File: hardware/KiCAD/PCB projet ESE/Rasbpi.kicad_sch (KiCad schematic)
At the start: 6 parts, among them J29 USB_C_Receptacle_USB2.0_16P, U5 USBLC6-2SC6

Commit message: maj schematic & pinout CubeIDE
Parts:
- renumbered J29 to J26, R30 to R22, R31 to R23
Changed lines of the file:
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@@
 		(dnp no)
 		(fields_autoplaced yes)
-		(property "Reference" "J29"
+		(property "Reference" "J26"
 			(at 90.17 69.85 0)
 			(effects
@@
 			(project ""
 				(path "/61bc2d2d-cd10-4636-b1b1-3d875f78e40b/7a080ce4-c82c-46c4-8a5a-914178d680a1"
-					(reference "J29")
+					(reference "J26")
 					(unit 1)
 				)
@@
 		(dnp no)
 		(fields_autoplaced yes)
-		(property "Reference" "#PWR0123"
+		(property "Reference" "#PWR0108"
 			(at 147.32 67.31 0)
 			(effects
@@
 			(project ""
 				(path "/61bc2d2d-cd10-4636-b1b1-3d875f78e40b/7a080ce4-c82c-46c4-8a5a-914178d680a1"
-					(reference "#PWR0123")
+					(reference "#PWR0108")
 					(unit 1)
 				)
@@
 		(dnp no)
 		(fields_autoplaced yes)
-		(property "Reference" "#PWR0121"
+		(property "Reference" "#PWR0106"
 			(at 124.46 91.44 0)
 			(effects
@@
 			(project ""
 				(path "/61bc2d2d-cd10-4636-b1b1-3d875f78e40b/7a080ce4-c82c-46c4-8a5a-914178d680a1"
-					(reference "#PWR0121")
+					(reference "#PWR0106")
 					(unit 1)
 				)
@@
 		(dnp no)
 		(fields_autoplaced yes)
-		(property "Reference" "#PWR0122"
+		(property "Reference" "#PWR0107"
 			(at 139.7 99.06 0)
 			(effects
@@
 			(project ""
 				(path "/61bc2d2d-cd10-4636-b1b1-3d875f78e40b/7a080ce4-c82c-46c4-8a5a-914178d680a1"
-					(reference "#PWR0122")
+					(reference "#PWR0107")
 					(unit 1)
 				)
@@
 		(on_board yes)
 		(dnp no)
-		(property "Reference" "R31"
+		(property "Reference" "R23"
 			(at 119.126 87.122 90)
 			(effects
@@
 			(project ""
 				(path "/61bc2d2d-cd10-4636-b1b1-3d875f78e40b/7a080ce4-c82c-46c4-8a5a-914178d680a1"
-					(reference "R31")
+					(reference "R23")
 					(unit 1)
 				)
@@
 		(dnp no)
 		(fields_autoplaced yes)
-		(property "Reference" "#PWR0120"
+		(property "Reference" "#PWR0105"
 			(at 86.36 121.92 0)
 			(effects
@@
 			(project ""
 				(path "/61bc2d2d-cd10-4636-b1b1-3d875f78e40b/7a080ce4-c82c-46c4-8a5a-914178d680a1"
-					(reference "#PWR0120")
+					(reference "#PWR0105")
 					(unit 1)
 				)
@@
 		(dnp no)
 		(fields_autoplaced yes)
-		(property "Reference" "R30"
+		(property "Reference" "R22"
 			(at 119.38 77.47 90)
 			(effects
@@
 			(project ""
 				(path "/61bc2d2d-cd10-4636-b1b1-3d875f78e40b/7a080ce4-c82c-46c4-8a5a-914178d680a1"
-					(reference "R30")
-					(unit 1)
-				)
+					(reference "R22")
+					(unit 1)
+				)

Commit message: maj
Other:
- moved on the sheet: F1, FB1, U5
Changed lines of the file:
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@@
 	(wire
 		(pts
-			(xy 123.19 63.5) (xy 134.62 63.5)
+			(xy 163.83 57.15) (xy 175.26 57.15)
 		)
 		(stroke
@@
 	(wire
 		(pts
-			(xy 147.32 63.5) (xy 139.7 63.5)
+			(xy 187.96 57.15) (xy 180.34 57.15)
 		)
 		(stroke
@@
 	(wire
 		(pts
-			(xy 118.11 63.5) (xy 115.57 63.5)
+			(xy 158.75 57.15) (xy 156.21 57.15)
 		)
 		(stroke
@@
 	(global_label "VBUS"
 		(shape input)
-		(at 115.57 63.5 180)
+		(at 156.21 57.15 180)
 		(fields_autoplaced yes)
 		(effects
@@
 		)
 		(property "Intersheetrefs" "${INTERSHEET_REFS}"
-			(at 107.2102 63.5 0)
+			(at 147.8502 57.15 0)
 			(effects
 				(font
@@
 	(global_label "D+"
 		(shape input)
-		(at 134.62 87.63 180)
+		(at 175.26 81.28 180)
 		(fields_autoplaced yes)
 		(effects
@@
 		)
 		(property "Intersheetrefs" "${INTERSHEET_REFS}"
-			(at 128.3164 87.63 0)
+			(at 168.9564 81.28 0)
 			(effects
 				(font
@@
 	(global_label "VBUS"
 		(shape input)
-		(at 139.7 80.01 90)
+		(at 180.34 73.66 90)
 		(fields_autoplaced yes)
 		(effects
@@
 		)
 		(property "Intersheetrefs" "${INTERSHEET_REFS}"
-			(at 139.7 71.6502 90)
+			(at 180.34 65.3002 90)
 			(effects
 				(font
@@
 	(global_label "D-"
 		(shape input)
-		(at 134.62 85.09 180)
+		(at 175.26 78.74 180)
 		(fields_autoplaced yes)
 		(effects
@@
 		)
 		(property "Intersheetrefs" "${INTERSHEET_REFS}"
-			(at 128.3164 85.09 0)
+			(at 168.9564 78.74 0)
 			(effects
 				(font
@@
 	(hierarchical_label "USB_DM"
 		(shape input)
-		(at 144.78 87.63 0)
+		(at 185.42 81.28 0)
 		(effects
 			(font
@@
 	(hierarchical_label "USB_DP"
 		(shape input)
-		(at 144.78 85.09 0)
+		(at 185.42 78.74 0)
 		(effects
 			(font
@@
 	(symbol
 		(lib_id "power:+5V")
-		(at 147.32 63.5 0)
+		(at 187.96 57.15 0)
 		(unit 1)
 		(exclude_from_sim no)
@@
 		(fields_autoplaced yes)
 		(property "Reference" "#PWR0108"
-			(at 147.32 67.31 0)
+			(at 187.96 60.96 0)
 			(effects
 				(font
@@
 		)
 		(property "Value" "+5V"
-			(at 147.32 58.42 0)
+			(at 187.96 52.07 0)
 			(effects
 				(font
@@
 		)
 		(property "Footprint" ""
-			(at 147.32 63.5 0)
+			(at 187.96 57.15 0)
 			(effects
 				(font
@@
 		)
 		(property "Datasheet" ""
-			(at 147.32 63.5 0)
+			(at 187.96 57.15 0)
 			(effects
 				(font
@@
 		)
 		(property "Description" "Power symbol creates a global label with name \"+5V\""
-			(at 147.32 63.5 0)
+			(at 187.96 57.15 0)
 			(effects
 				(font
@@
 	(symbol
 		(lib_id "Device:FerriteBead_Small")
-		(at 120.65 63.5 90)
+		(at 161.29 57.15 90)
 		(unit 1)
 		(exclude_from_sim no)
@@
 		(fields_autoplaced yes)
 		(property "Reference" "FB1"
-			(at 120.6119 57.15 90)
+			(at 161.2519 50.8 90)
 			(effects
 				(font
@@
 		)
 		(property "Value" "600 @ 100MHz"
-			(at 120.6119 59.69 90)
+			(at 161.2519 53.34 90)
 			(effects
 				(font
@@
 		)
 		(property "Footprint" "Inductor_SMD:L_0805_2012Metric"
-			(at 120.65 65.278 90)
+			(at 161.29 58.928 90)
 			(effects
 				(font
@@
 		)
 		(property "Datasheet" "~"
-			(at 120.65 63.5 0)
+			(at 161.29 57.15 0)
 			(effects
 				(font
@@
 		)
 		(property "Description" "Ferrite bead, small symbol"
-			(at 120.65 63.5 0)
+			(at 161.29 57.15 0)
 			(effects
 				(font
@@
 	(symbol
 		(lib_id "Device:Polyfuse_Small")
-		(at 137.16 63.5 90)
+		(at 177.8 57.15 90)
 		(unit 1)
 		(exclude_from_sim no)
@@
 		(fields_autoplaced yes)
 		(property "Reference" "F1"
-			(at 137.16 57.15 90)
+			(at 177.8 50.8 90)
 			(effects
 				(font
@@
 		)
 		(property "Value" "250mA"
-			(at 137.16 59.69 90)
+			(at 177.8 53.34 90)
 			(effects
 				(font
@@
 		)
 		(property "Footprint" "Fuse:Fuse_1206_3216Metric"
-			(at 142.24 62.23 0)
+			(at 182.88 55.88 0)
 			(effects
 				(font
@@
 		)
 		(property "Datasheet" "~"
-			(at 137.16 63.5 0)
+			(at 177.8 57.15 0)
 			(effects
 				(font
@@
 		)
 		(property "Description" "Resettable fuse, polymeric positive temperature coefficient, small symbol"
-			(at 137.16 63.5 0)
+			(at 177.8 57.15 0)
 			(effects
 				(font
@@
 	(symbol
 		(lib_id "power:GND")
-		(at 139.7 92.71 0)
+		(at 180.34 86.36 0)
 		(unit 1)
 		(exclude_from_sim no)
@@
 		(fields_autoplaced yes)
 		(property "Reference" "#PWR0107"
-			(at 139.7 99.06 0)
+			(at 180.34 92.71 0)
 			(effects
 				(font
@@
 		)
 		(property "Value" "GND"
-			(at 139.7 97.79 0)
+			(at 180.34 91.44 0)
 			(effects
 				(font
@@
 		)
 		(property "Footprint" ""
-			(at 139.7 92.71 0)
+			(at 180.34 86.36 0)
 			(effects
 				(font
@@
 		)
 		(property "Datasheet" ""
-			(at 139.7 92.71 0)
+			(at 180.34 86.36 0)
 			(effects
 				(font
@@
 		)
 		(property "Description" "Power symbol creates a global label with name \"GND\" , ground"
-			(at 139.7 92.71 0)
+			(at 180.34 86.36 0)
 			(effects
 				(font
@@
 	(symbol
 		(lib_id "Power_Protection:USBLC6-2SC6")
-		(at 139.7 85.09 0)
+		(at 180.34 78.74 0)
 		(unit 1)
 		(exclude_from_sim no)
@@
 		(fields_autoplaced yes)
 		(property "Reference" "U5"
-			(at 141.3511 77.47 0)
+			(at 181.9911 71.12 0)
 			(effects
 				(font
@@
 		)
 		(property "Value" "USBLC6-2SC6"
-			(at 141.3511 80.01 0)
+			(at 181.9911 73.66 0)
 			(effects
 				(font
@@
 		)
 		(property "Footprint" "Package_TO_SOT_SMD:SOT-23-6"
-			(at 140.97 91.44 0)
+			(at 181.61 85.09 0)
 			(effects
 				(font
@@
 		)
 		(property "Datasheet" "https://www.st.com/resource/en/datasheet/usblc6-2.pdf"
-			(at 140.97 93.345 0)
+			(at 181.61 86.995 0)
 			(effects
 				(font
@@
 		)
 		(property "Description" "Very low capacitance ESD protection diode, 2 data-line, SOT-23-6"
-			(at 139.7 85.09 0)
+			(at 180.34 78.74 0)
 			(effects
 				(font
@@
 		)
 		(property "MPN" "624-7693"
-			(at 139.7 85.09 0)
-			(effects
-				(font
+			(at 180.34 78.74 0)
+			(effects
+				(font

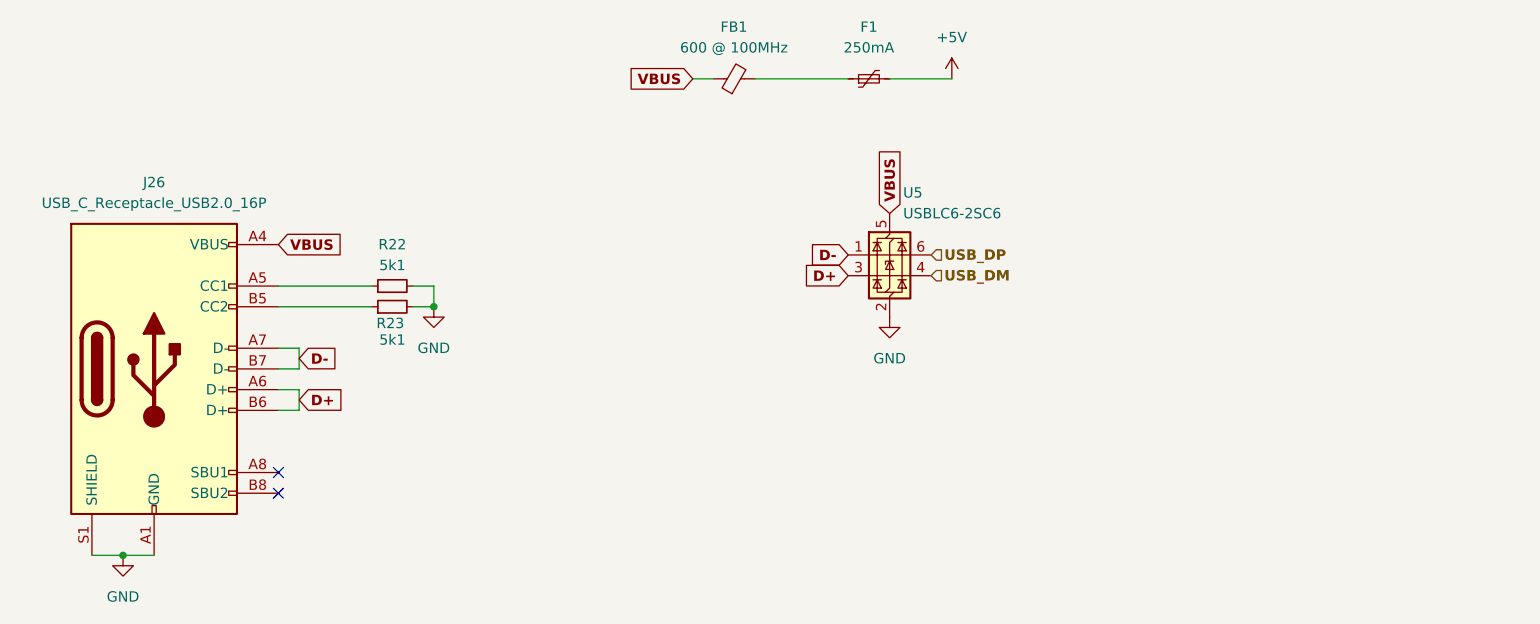
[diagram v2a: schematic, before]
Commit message: replace usb c by jst xh
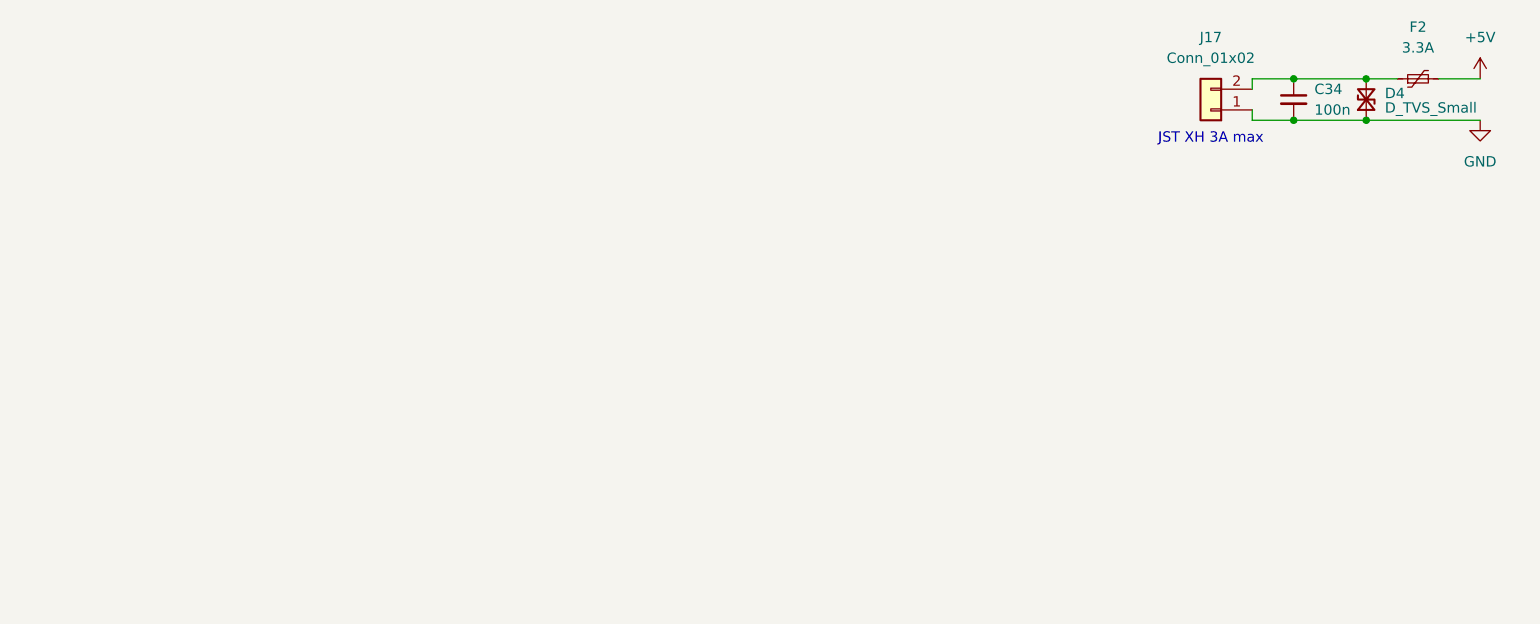
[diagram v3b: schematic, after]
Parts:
- removed F1: 250mA, Fuse:Fuse_1206_3216Metric, symbol Device:Polyfuse_Small
- removed FB1: 600 @ 100MHz, Inductor_SMD:L_0805_2012Metric, symbol Device:FerriteBead_Small
- removed J26: USB_C_Receptacle_USB2.0_16P, Connector_USB:USB_C_Receptacle_HRO_TYPE-C-31-M-12, symbol Connector:USB_C_Receptacle_USB2.0_16P
- removed R22, R23: 5k1, Resistor_SMD:R_0402_1005Metric, symbol Device:R_Small
- removed U5: USBLC6-2SC6, Package_TO_SOT_SMD:SOT-23-6, symbol Power_Protection:USBLC6-2SC6
- added C34: 100n, Capacitor_SMD:C_0402_1005Metric, symbol Device:C_Small
- added D4: D_TVS_Small, Diode_SMD:D_SOD-523, symbol Device:D_TVS_Small
- added F2: 3.3A, Fuse:Fuse_2920_7451Metric, symbol Device:Polyfuse_Small
- added J17: Conn_01x02, Connector_JST:JST_XH_B2B-XH-A_1x02_P2.50mm_Vertical, symbol Connector_Generic:Conn_01x02
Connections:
- net +5V: now also F2.2
- net GND: now also C34.2, D4.1 (A1), J17.1 (Pin_1)
- new net: C34.1, D4.2 (A2), F2.1, J17.2 (Pin_2)
- no-connect marks 2 -> 0
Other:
- note added: "JST XH 3A max"

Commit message: v1 PCB
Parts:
- added C35: 10u, Capacitor_SMD:C_0402_1005Metric, symbol Device:C_Small
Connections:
- net GND: now also C35.2
- net at C34.1, D4.2 (A2), F2.1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: now also C35.1
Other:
- moved on the sheet: C34, D4
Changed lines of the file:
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@@
 	)
 	(junction
-		(at 238.76 57.15)
+		(at 233.68 62.23)
 		(diameter 0)
 		(color 0 0 0 0)
 	)
 	(junction
-		(at 229.87 57.15)
+		(at 233.68 57.15)
 		(diameter 0)
 		(color 0 0 0 0)
 	)
 	(junction
-		(at 238.76 62.23)
+		(at 241.3 62.23)
 		(diameter 0)
 		(color 0 0 0 0)
 	)
 	(junction
-		(at 229.87 62.23)
+		(at 227.33 57.15)
 		(diameter 0)
 		(color 0 0 0 0)
 	)
+	(junction
+		(at 227.33 62.23)
+		(diameter 0)
+		(color 0 0 0 0)
+	)
+	(junction
+		(at 241.3 57.15)
+		(diameter 0)
+		(color 0 0 0 0)
+	)
 	(wire
 		(pts
@@
 	(wire
 		(pts
-			(xy 229.87 62.23) (xy 238.76 62.23)
-		)
-		(stroke
-			(width 0)
-			(type default)
-		)
-	)
-	(wire
-		(pts
-			(xy 238.76 57.15) (xy 242.57 57.15)
-		)
-		(stroke
-			(width 0)
-			(type default)
-		)
-	)
-	(wire
-		(pts
-			(xy 229.87 57.15) (xy 224.79 57.15)
+			(xy 227.33 62.23) (xy 233.68 62.23)
+		)
+		(stroke
+			(width 0)
+			(type default)
+		)
+	)
+	(wire
+		(pts
+			(xy 241.3 62.23) (xy 252.73 62.23)
+		)
+		(stroke
+			(width 0)
+			(type default)
+		)
+	)
+	(wire
+		(pts
+			(xy 227.33 57.15) (xy 233.68 57.15)
 		)
 		(stroke
@@
 	(wire
 		(pts
-			(xy 238.76 62.23) (xy 252.73 62.23)
-		)
-		(stroke
-			(width 0)
-			(type default)
-		)
-	)
-	(wire
-		(pts
-			(xy 224.79 62.23) (xy 229.87 62.23)
+			(xy 233.68 62.23) (xy 241.3 62.23)
+		)
+		(stroke
+			(width 0)
+			(type default)
+		)
+	)
+	(wire
+		(pts
+			(xy 241.3 57.15) (xy 242.57 57.15)
+		)
+		(stroke
+			(width 0)
+			(type default)
+		)
+	)
+	(wire
+		(pts
+			(xy 224.79 62.23) (xy 227.33 62.23)
+		)
+		(stroke
+			(width 0)
+			(type default)
+		)
+	)
+	(wire
+		(pts
+			(xy 233.68 57.15) (xy 241.3 57.15)
+		)
+		(stroke
+			(width 0)
+			(type default)
+		)
+	)
+	(wire
+		(pts
+			(xy 227.33 57.15) (xy 224.79 57.15)
 		)
 		(stroke
@@
 		(pts
 			(xy 224.79 57.15) (xy 224.79 58.42)
-		)
-		(stroke
-			(width 0)
-			(type default)
-		)
-	)
-	(wire
-		(pts
-			(xy 229.87 57.15) (xy 238.76 57.15)
 		)
 		(stroke
@@
 	(symbol
 		(lib_id "Device:C_Small")
-		(at 229.87 59.69 0)
+		(at 233.68 59.69 0)
+		(unit 1)
+		(exclude_from_sim no)
+		(in_bom yes)
+		(on_board yes)
+		(dnp no)
+		(property "Reference" "C35"
+			(at 236.22 58.4262 0)
+			(effects
+				(font
+					(size 1.27 1.27)
+				)
+				(justify left)
+			)
+		)
+		(property "Value" "10u"
+			(at 236.22 60.96 0)
+			(effects
+				(font
+					(size 1.27 1.27)
+				)
+				(justify left)
+			)
+		)
+		(property "Footprint" "Capacitor_SMD:C_0402_1005Metric"
+			(at 233.68 59.69 0)
+			(effects
+				(font
+					(size 1.27 1.27)
+				)
+				(hide yes)
+			)
+		)
+		(property "Datasheet" "~"
+			(at 233.68 59.69 0)
+			(effects
+				(font
+					(size 1.27 1.27)
+				)
+				(hide yes)
+			)
+		)
+		(property "Description" "Unpolarized capacitor, small symbol"
+			(at 233.68 59.69 0)
+			(effects
+				(font
+					(size 1.27 1.27)
+				)
+				(hide yes)
+			)
+		)
+		(pin "1"
+		)
+		(pin "2"
+		)
+		(instances
+			(project "PCB projet ESE"
+				(path "/61bc2d2d-cd10-4636-b1b1-3d875f78e40b/7a080ce4-c82c-46c4-8a5a-914178d680a1"
+					(reference "C35")
+					(unit 1)
+				)
+			)
+		)
+	)
+	(symbol
+		(lib_id "Device:C_Small")
+		(at 227.33 59.69 0)
 		(unit 1)
 		(exclude_from_sim no)
@@
 		(dnp no)
 		(property "Reference" "C34"
-			(at 232.41 58.4262 0)
+			(at 229.87 58.4262 0)
 			(effects
 				(font
@@
 		)
 		(property "Value" "100n"
-			(at 232.41 60.96 0)
+			(at 229.87 60.96 0)
 			(effects
 				(font
@@
 		)
 		(property "Footprint" "Capacitor_SMD:C_0402_1005Metric"
-			(at 229.87 59.69 0)
+			(at 227.33 59.69 0)
 			(effects
 				(font
@@
 		)
 		(property "Datasheet" "~"
-			(at 229.87 59.69 0)
+			(at 227.33 59.69 0)
 			(effects
 				(font
@@
 		)
 		(property "Description" "Unpolarized capacitor, small symbol"
-			(at 229.87 59.69 0)
+			(at 227.33 59.69 0)
 			(effects
 				(font
@@
 	(symbol
 		(lib_id "Device:D_TVS_Small")
-		(at 238.76 59.69 90)
+		(at 241.3 59.69 90)
 		(unit 1)
 		(exclude_from_sim no)
@@
 		(dnp no)
 		(property "Reference" "D4"
-			(at 241.046 58.928 90)
+			(at 243.586 58.928 90)
 			(effects
 				(font
@@
 		)
 		(property "Value" "D_TVS_Small"
-			(at 241.046 60.706 90)
+			(at 243.586 60.706 90)
 			(effects
 				(font
@@
 		)
 		(property "Footprint" "Diode_SMD:D_SOD-523"
-			(at 238.76 59.69 0)
+			(at 241.3 59.69 0)
 			(effects
 				(font
@@
 		)
 		(property "Datasheet" "~"
-			(at 238.76 59.69 0)
+			(at 241.3 59.69 0)
 			(effects
 				(font
@@
 		)
 		(property "Description" "Bidirectional transient-voltage-suppression diode, small symbol"
-			(at 238.76 59.69 0)
-			(effects
-				(font
+			(at 241.3 59.69 0)
+			(effects
+				(font
